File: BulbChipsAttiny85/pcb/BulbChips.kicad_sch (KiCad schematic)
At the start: 5 parts, among them SW1 SW_Push, U1 ATtiny85-20P

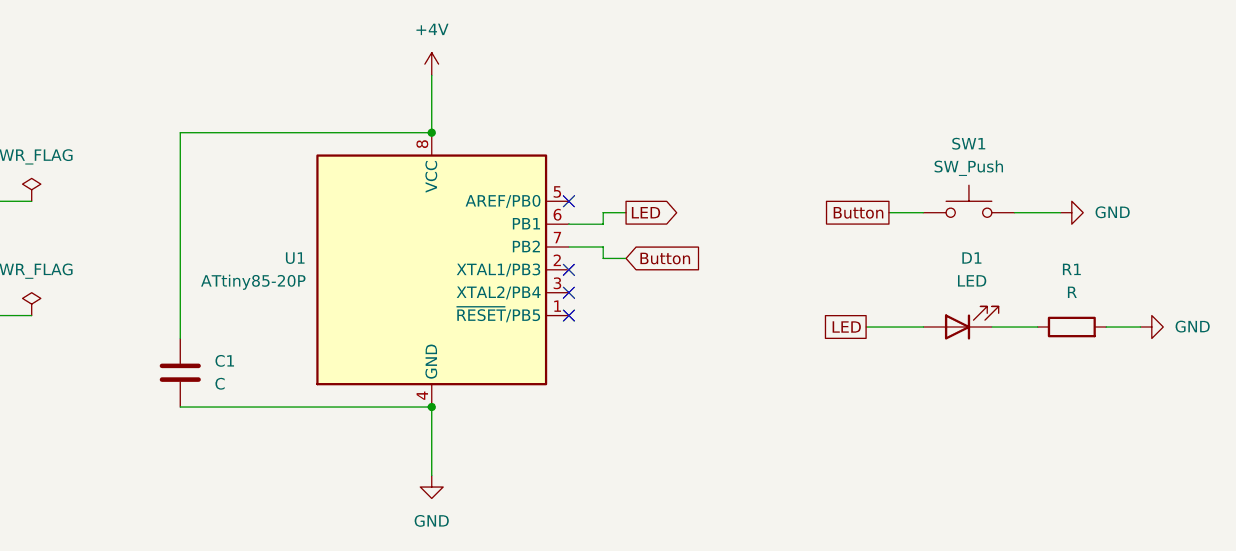
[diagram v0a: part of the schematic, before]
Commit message: changed attiny85 to QFP package
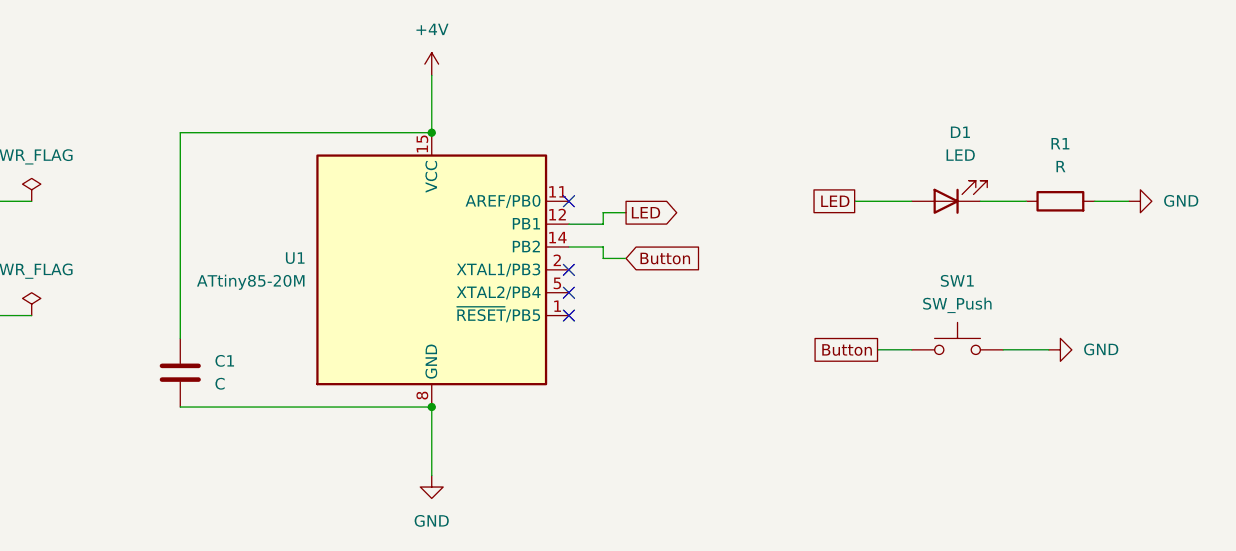
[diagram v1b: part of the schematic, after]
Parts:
- removed U1: ATtiny85-20P, Package_DIP:DIP-8_W7.62mm, symbol MCU_Microchip_ATtiny:ATtiny85-20P
- added U1: ATtiny85-20M, Package_DFN_QFN:QFN-20-1EP_4x4mm_P0.5mm_EP2.6x2.6mm, symbol MCU_Microchip_ATtiny:ATtiny85-20M
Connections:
- net +4V: now also U1.15 (VCC)
- net Button: now also U1.14 (PB2)
- net GND: now also U1.21 (GND), U1.8 (GND)
- net LED: now also U1.12 (PB1)
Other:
- moved on the sheet: D1, R1, SW1

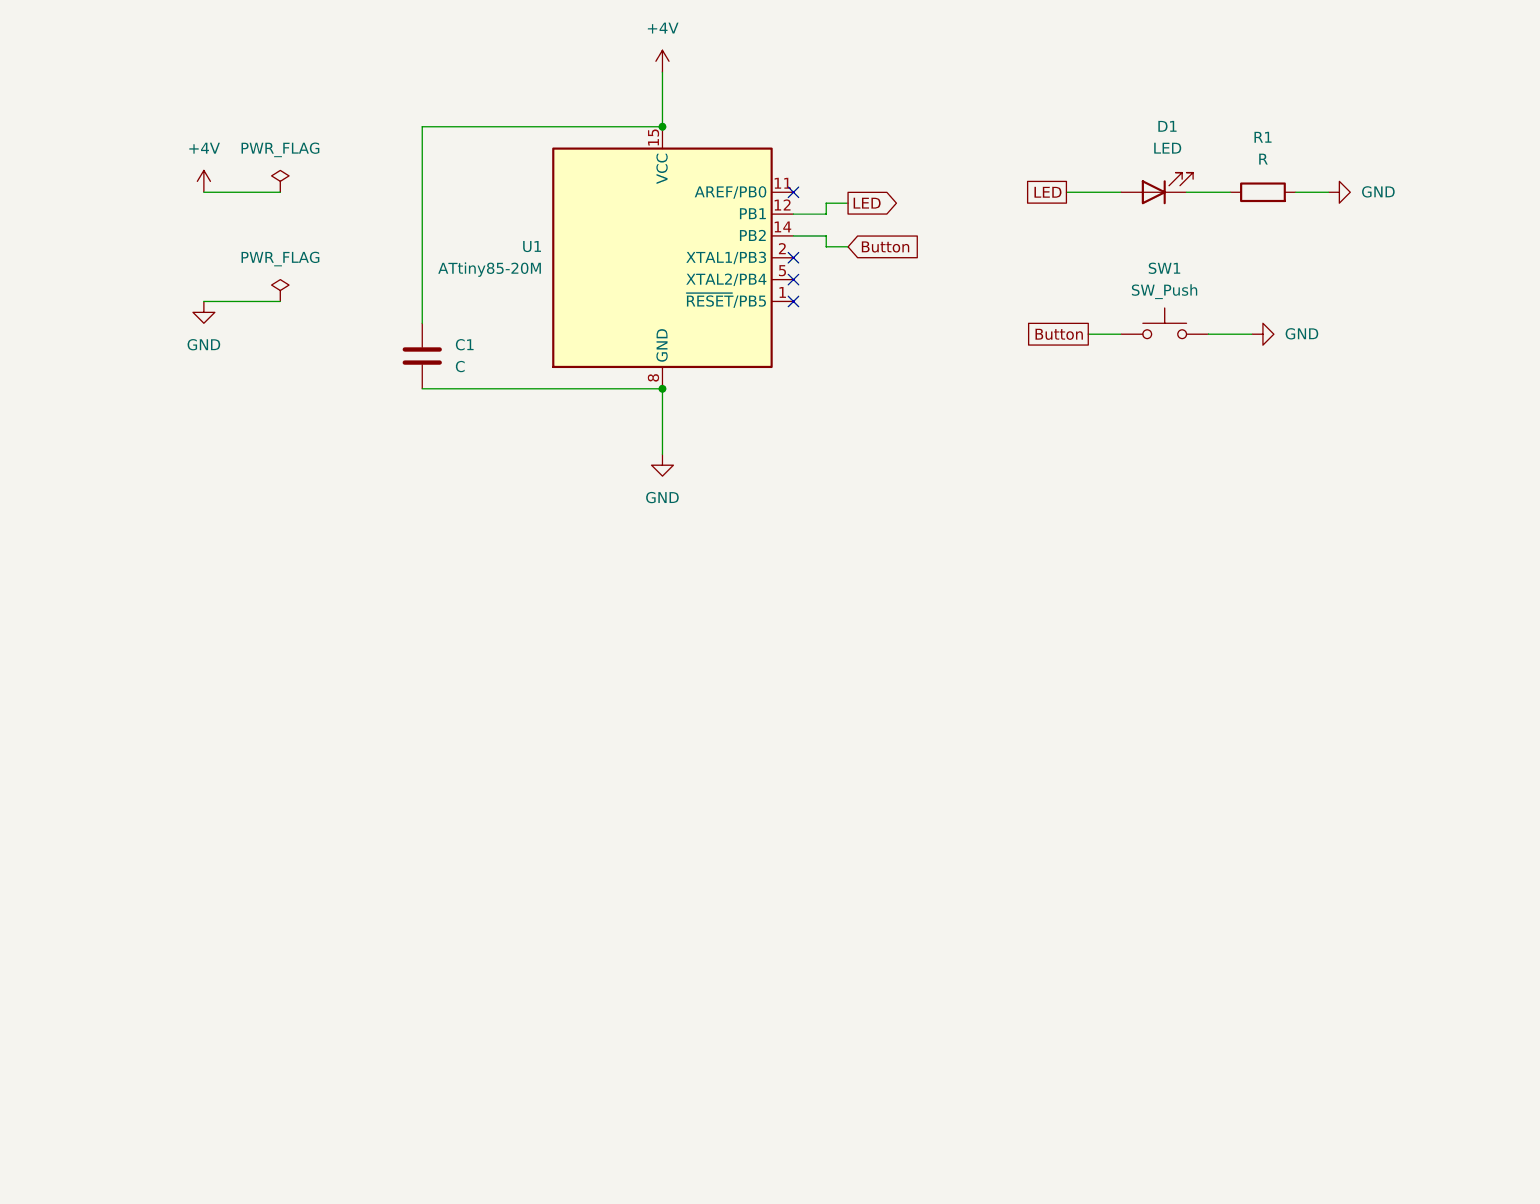
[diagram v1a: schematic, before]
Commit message: adding usb connection to schematic, tx2- and tx2+ hijacked to potentially program it over usb connections using SPI protocol, before attiny has any software on it
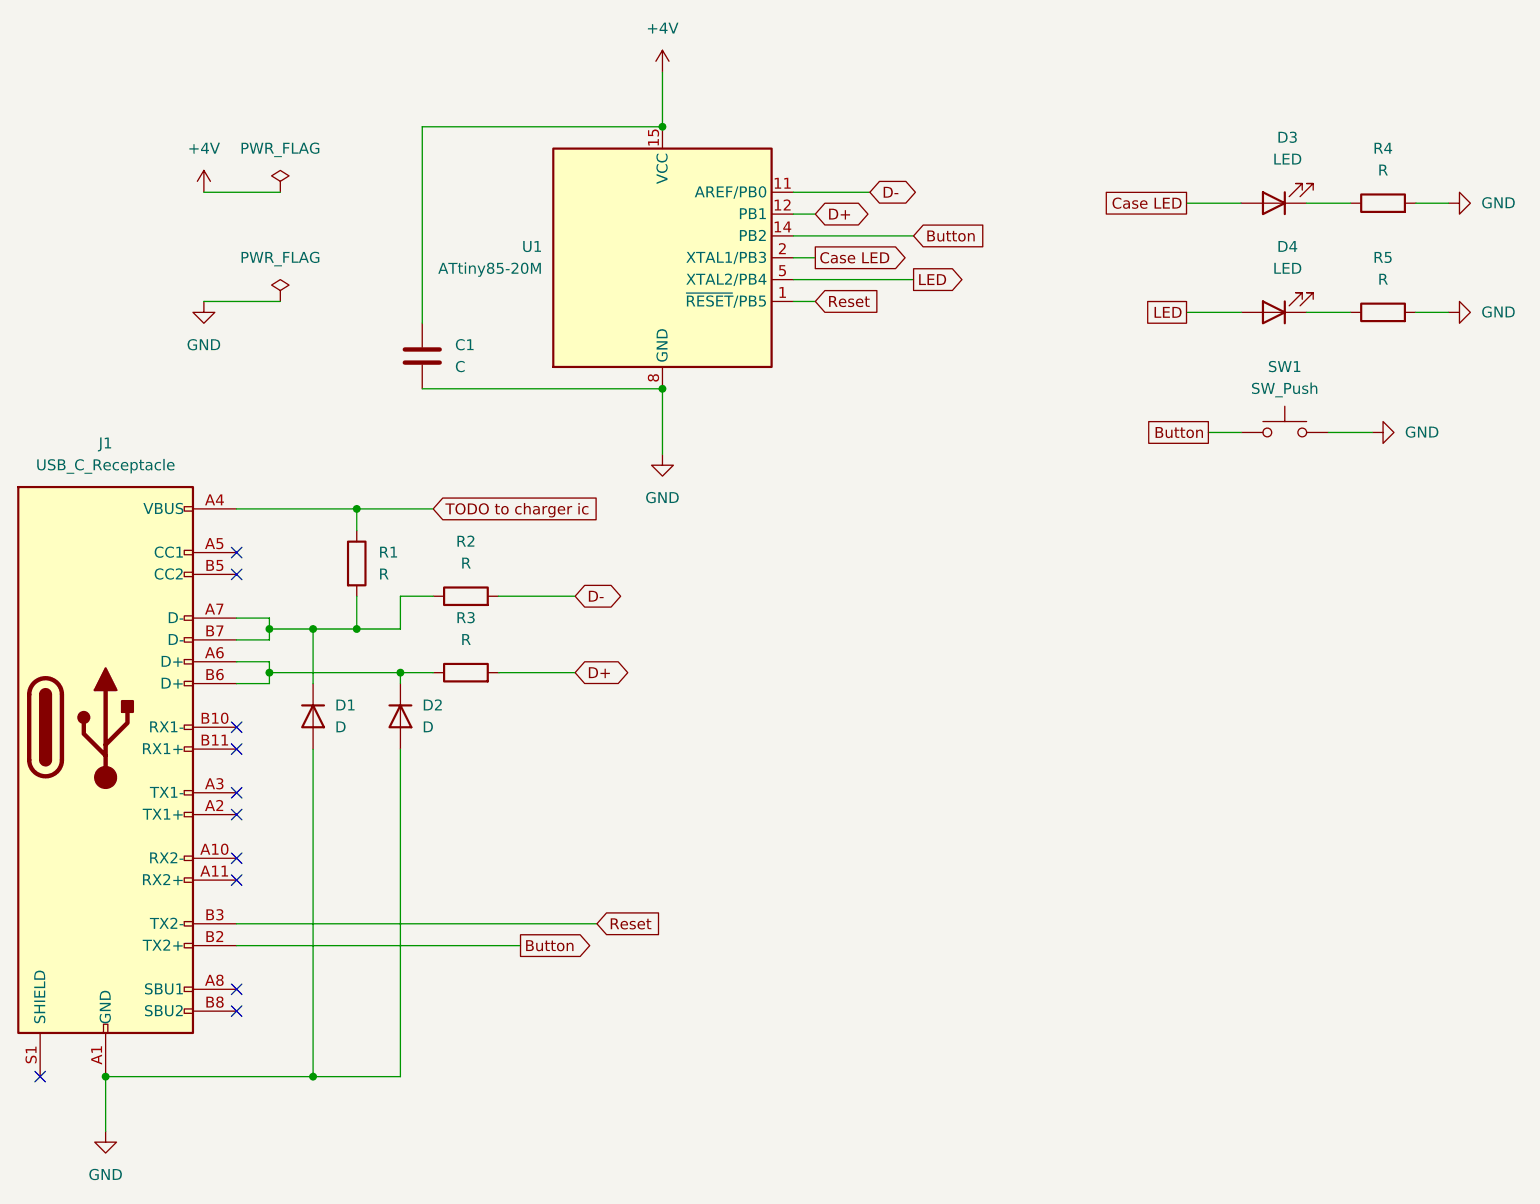
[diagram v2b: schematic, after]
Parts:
- added D1, D2: D, symbol Device:D
- added D3: LED, symbol Device:LED
- added J1: USB_C_Receptacle, symbol Connector:USB_C_Receptacle
- added R1, R2, R3, R4: R, symbol Device:R
- renumbered D1 to D4, R1 to R5
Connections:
- net Button: now also J1.B2 (TX2+)
- net GND: now also D1.2 (A), D2.2 (A), J1.A1 (GND), J1.A12 (GND), J1.B1 (GND), J1.B12 (GND), R4.2
- net LED: now also U1.5 (XTAL2/PB4); no longer U1.12 (PB1)
- net Reset: now reaches U1.1 (~{RESET}/PB5)
- net Reset: now also J1.B3 (TX2-)
- net D-: now reaches U1.11 (AREF/PB0)
- net D-: now also R2.2
- net Case LED: now reaches U1.2 (XTAL1/PB3)
- net Case LED: now also D3.2 (A)
- new net: D1.1 (K), J1.A7 (D-), J1.B7 (D-), R1.2, R2.1
- new net: D2.1 (K), J1.A6 (D+), J1.B6 (D+), R3.1
- new net: D3.1 (K), R4.1
- new net D+: R3.2, U1.12 (PB1)
- new net TODO to charger ic: J1.A4 (VBUS), J1.A9 (VBUS), J1.B4 (VBUS), J1.B9 (VBUS), R1.1
- no-connect marks 4 -> 11
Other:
- moved on the sheet: D4, R5, SW1

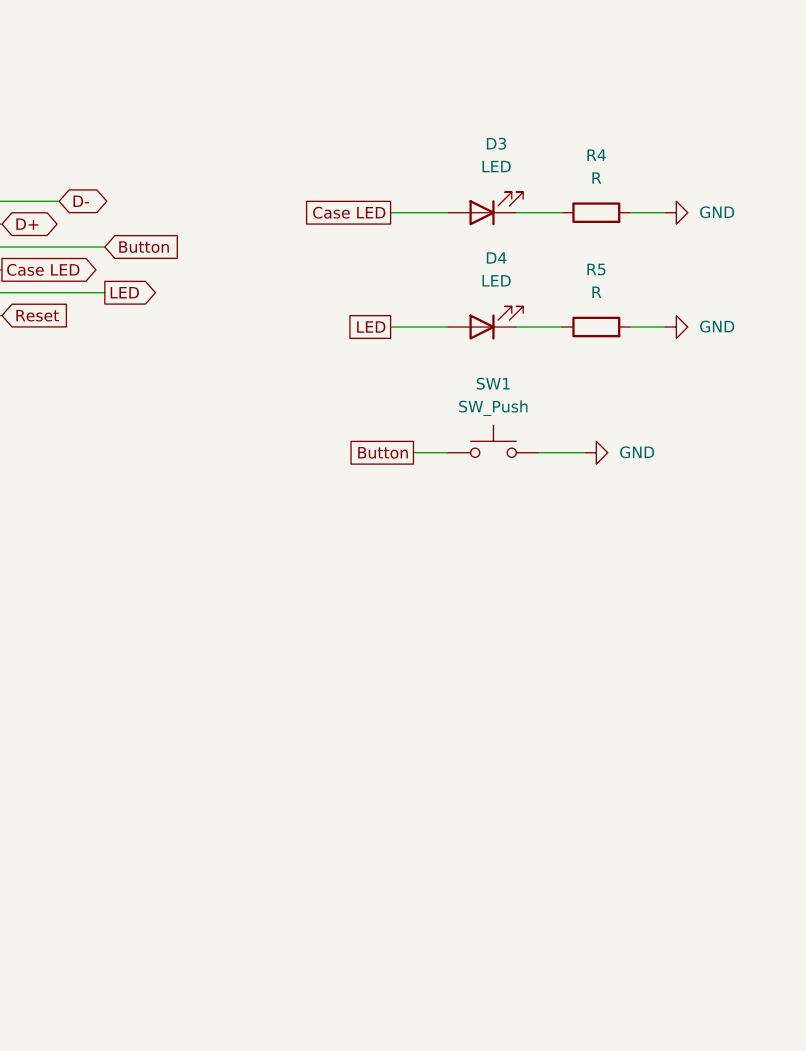
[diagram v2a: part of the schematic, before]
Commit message: got symbol for BQ24040DSQR charger added, still need to make changes to be BQ24045DSQR ic instead
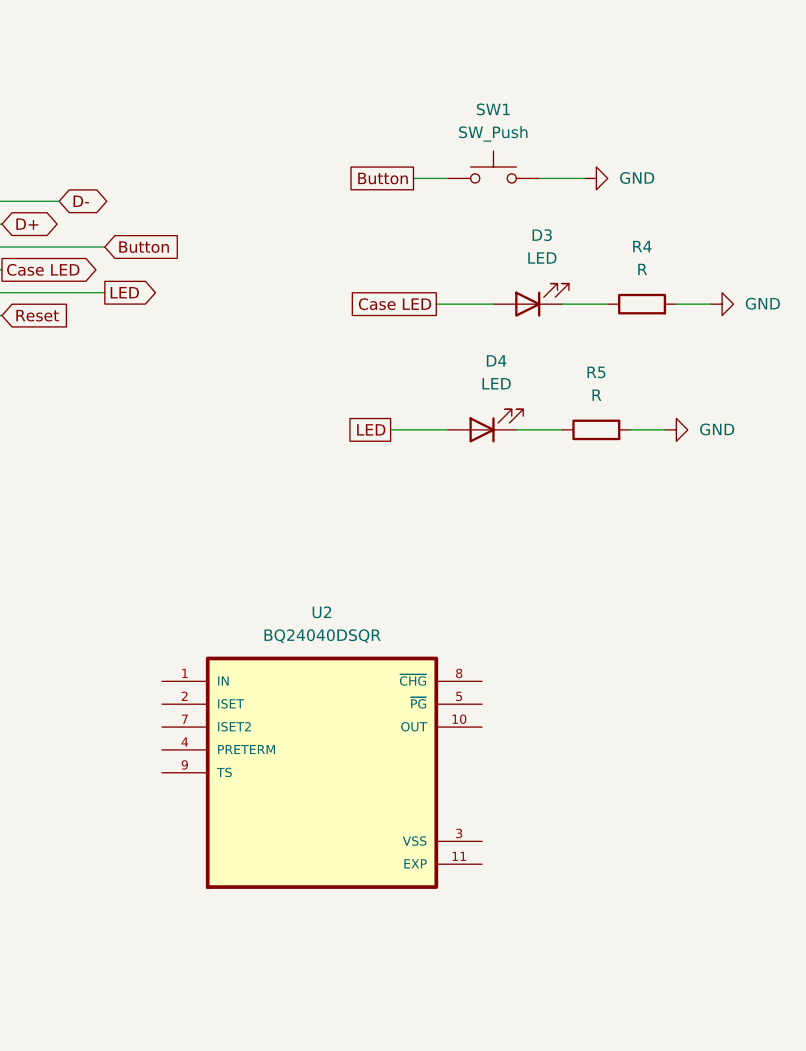
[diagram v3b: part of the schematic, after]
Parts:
- added U2: BQ24040DSQR, BQ24040DSQR:SON40P200X200X80-11N, symbol BQ24040DSQR:BQ24040DSQR
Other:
- moved on the sheet: D3, D4, R4, R5, SW1

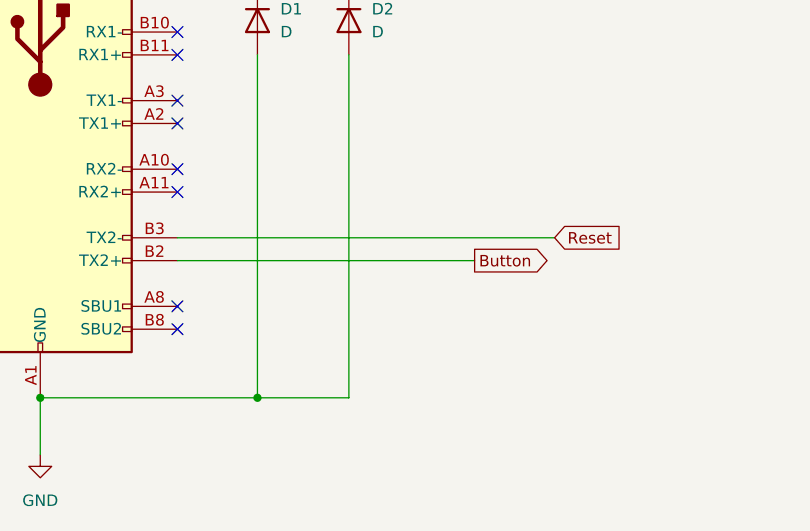
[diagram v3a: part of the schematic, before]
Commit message: moved spi programming pins to usb SBU1 and SBU2
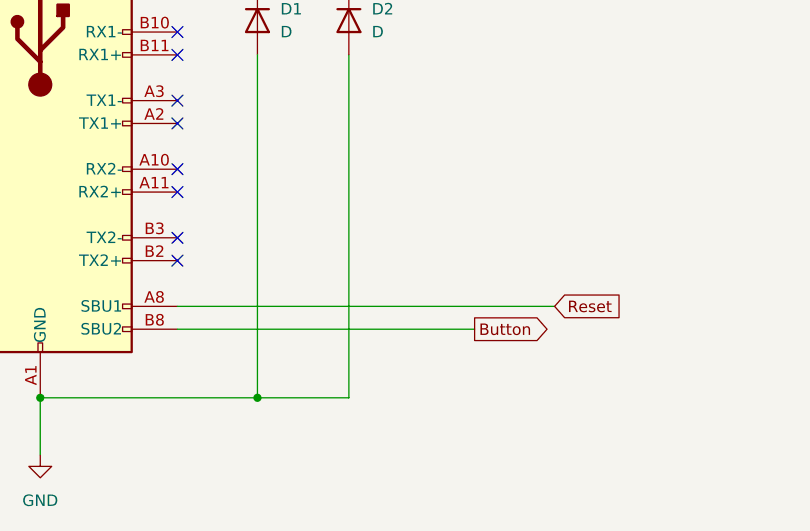
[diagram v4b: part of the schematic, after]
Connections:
- net Button: now also J1.B8 (SBU2); no longer J1.B2 (TX2+)
- net Reset: now also J1.A8 (SBU1); no longer J1.B3 (TX2-)
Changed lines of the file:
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@@
-	)
-	(no_connect
-		(at 52.07 172.72)
 	)
 	(no_connect
@@
 	)
 	(no_connect
-		(at 52.07 170.18)
+		(at 52.07 165.1)
 	)
 	(no_connect
@@
 		(at 29.21 180.34)
 	)
+	(no_connect
+		(at 52.07 162.56)
+	)
+	(wire
+		(pts
+			(xy 52.07 170.18) (xy 93.98 170.18)
+		)
+		(stroke
+			(width 0)
+			(type default)
+		)
+	)
 	(wire
 		(pts
@@
 	(wire
 		(pts
-			(xy 52.07 165.1) (xy 85.09 165.1)
-		)
-		(stroke
-			(width 0)
-			(type default)
-		)
-	)
-	(wire
-		(pts
 			(xy 71.12 142.24) (xy 71.12 180.34)
 		)
@@
 	(wire
 		(pts
+			(xy 52.07 172.72) (xy 85.09 172.72)
+		)
+		(stroke
+			(width 0)
+			(type default)
+		)
+	)
+	(wire
+		(pts
 			(xy 55.88 127) (xy 55.88 128.27)
 		)
@@
 		(pts
 			(xy 179.07 74.93) (xy 184.15 74.93)
-		)
-		(stroke
-			(width 0)
-			(type default)
-		)
-	)
-	(wire
-		(pts
-			(xy 52.07 162.56) (xy 93.98 162.56)
 		)
 		(stroke
@@
 	(global_label "Button"
 		(shape output)
-		(at 85.09 165.1 0)
-		(fields_autoplaced yes)
-		(effects
-			(font
-				(size 1.27 1.27)
-			)
-			(justify left)
-		)
-		(property "Intersheetrefs" "${INTERSHEET_REFS}"
-			(at 94.2436 165.1 0)
+		(at 85.09 172.72 0)
+		(fields_autoplaced yes)
+		(effects
+			(font
+				(size 1.27 1.27)
+			)
+			(justify left)
+		)
+		(property "Intersheetrefs" "${INTERSHEET_REFS}"
+			(at 94.2436 172.72 0)
 			(effects
 				(font
@@
 	(global_label "Reset"
 		(shape input)
-		(at 93.98 162.56 0)
-		(fields_autoplaced yes)
-		(effects
-			(font
-				(size 1.27 1.27)
-			)
-			(justify left)
-		)
-		(property "Intersheetrefs" "${INTERSHEET_REFS}"
-			(at 102.1662 162.56 0)
-			(effects
-				(font
+		(at 93.98 170.18 0)
+		(fields_autoplaced yes)
+		(effects
+			(font
+				(size 1.27 1.27)
+			)
+			(justify left)
+		)
+		(property "Intersheetrefs" "${INTERSHEET_REFS}"
+			(at 102.1662 170.18 0)
+			(effects
+				(font
